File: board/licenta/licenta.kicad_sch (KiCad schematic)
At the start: 44 parts, among them IC1 SAMACSYS_PARTS_NCP186BMX330TAG, IC2 SAMACSYS_PARTS_ESP32-C3-WROOM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, IC3 SAMACSYS_PARTS_BMI085, J1 SAMACSYS_PARTS_USB4110-GF-A, J2 SAMACSYS_PARTS_112A-TAAR-R03_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, Q1 ESP32_WROVER_SPARKFUN-DISCRET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, U1 ESP32-C3-MINI-1, U2 ESP32_WROVER_SPARKFUN-IC-POWE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, U3 DRV2605LDGS, U4 GC9A01_IPS_display_SPI

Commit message: Update schematics w/o PPG
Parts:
- removed IC2: SAMACSYS_PARTS_ESP32-C3-WROOM-02-H4, mini_iot:SAMACSYS_PARTS_ESP32C3WROOM02H4, symbol mini_iot-eagle-import:SAMACSYS_PARTS_ESP32-C3-WROOM-02-H4
- added C1_BAT3: 0.1uF, mini_iot:ESP32_WROVER_EAGLE-LTSPICE_C0402, symbol mini_iot-eagle-import:ESP32_WROVER_EAGLE-LTSPICE_CC0402
- added C1_DRV, C1_DRV1: 1.0uF, mini_iot:ESP32_WROVER_EAGLE-LTSPICE_C0402, symbol mini_iot-eagle-import:ESP32_WROVER_EAGLE-LTSPICE_CC0402
- added C3, C4, C5: 1uF, mini_iot:ESP32_WROVER_EAGLE-LTSPICE_C0402, symbol mini_iot-eagle-import:ESP32_WROVER_EAGLE-LTSPICE_CC0402
- added Q2: 2N7002, Package_TO_SOT_SMD:SOT-23, symbol Transistor_FET:2N7002
- added R1_BTN, R1_ESP1, R2_BTN1, R3_BTN2: 10k, mini_iot:ESP32_WROVER_EAGLE-LTSPICE_R0402, symbol mini_iot-eagle-import:ESP32_WROVER_EAGLE-LTSPICE_RR0402
- added R1_DRV2, R2_DRV2: 2.2k, mini_iot:ESP32_WROVER_EAGLE-LTSPICE_R0402, symbol mini_iot-eagle-import:ESP32_WROVER_EAGLE-LTSPICE_RR0402
- added R1_ESP: 22, mini_iot:ESP32_WROVER_EAGLE-LTSPICE_R0402, symbol mini_iot-eagle-import:ESP32_WROVER_EAGLE-LTSPICE_RR0402
- added SW1: BUTTON_1, Button_Switch_THT:SW_PUSH_LCD_E3_SAxxxx, symbol Switch:SW_MEC_5E
- added SW2: BUTTON_2, Button_Switch_THT:SW_PUSH_LCD_E3_SAxxxx, symbol Switch:SW_MEC_5E
- added SW3: BUTTON_3, Button_Switch_THT:SW_PUSH_LCD_E3_SAxxxx, symbol Switch:SW_MEC_5E
- added U5: A1027, symbol licenta:A1027
- R1_ESP3: value 10k -> 1M
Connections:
- net A1 is gone; now on net ADC_BAT: SJ3.1
- net SDA is gone; now on net 3V3: IC3.9 (SDA/SDI), LED2.6 (SDA)
- net 3V3: now also U1.23 (GPIO9), U1.3 (3V3), U3.10 (VDD), U3.3 (SDA), U4.4 (VDD), C1_BAT3.1, C1_DRV1.2, R1_BTN.2, R1_DRV2.2, R1_ESP.1, R1_ESP1.2, R2_BTN1.2, R2_DRV2.1, R3_BTN2.2; no longer R1_ESP2.2, R1_ESP3.2
- net D+: now also U1.27 (GPIO19/USB_D+)
- net D-: now also U1.26 (GPIO18/USB_D-)
- net GND: now also R1_ESP3.2, U1.1 (GND), U1.11 (GND), U1.14 (GND), U1.2 (GND), U1.36 (GND), U1.37 (GND), U1.38 (GND), U1.39 (GND), U1.40 (GND), U1.41 (GND), U1.42 (GND), U1.43 (GND), U1.44 (GND), U1.45 (GND), U1.46 (GND), U1.47 (GND), U1.48 (GND), U1.49 (GND), U1.50 (GND), U1.51 (GND), U1.52 (GND), U1.53 (GND), U3.8 (GND), U4.1 (GND), U4.12 (GND), U4.5 (GND), U4.6 (GND), C1_BAT3.2, C1_DRV.1, C1_DRV1.1, C3.1, C4.1, C5.1, Q2.2 (S), SW1.1, SW1.2, SW2.1, SW2.2, SW3.1, SW3.2
- net GPIO1: now also U1.13 (GPIO1/ADC1_CH1/XTAL_32K_N)
- net MISO: now also U1.5 (GPIO2/ADC1_CH2), R1_ESP1.1; no longer R1_ESP2.1
- net MOSI: now also U1.21 (GPIO7), U4.10 (SDI)
- net SCK: now also U1.20 (GPIO6), U4.9 (SCK)
- net SCL: now also U1.22 (GPIO8), U3.2 (SCL), R2_DRV2.2
- net SS: no longer J2.P2 (CD/DAT3)
- net SS_SD: now reaches U1.16 (GPIO10)
- net SS_SD: now also J2.P2 (CD/DAT3)
- net TFT_DC: now reaches U1.19 (GPIO5/ADC2_CH0)
- net TFT_DC: now also U4.7 (D/C)
- net SS_TFT: now reaches U1.30 (GPIO20/U0RXD)
- net SS_TFT: now also U4.8 (~{CS})
- net ADC_BAT: now reaches U1.6 (GPIO3/ADC1_CH3)
- net at U3.1 (REG): now also C1_DRV.2
- net IN_DRV: now reaches U3.4 (IN/TRIG)
- net EN_DRV: now reaches U3.5 (EN)
- net OUT+: now reaches U3.7 (OUT+)
- net OUT+: now also U5.1 (OUT+)
- net OUT-: now reaches U3.9 (OUT-)
- net OUT-: now also U5.2 (OUT-)
- net DISP_RST: now reaches U4.11 (~{RESET})
- net LEDK: now reaches U4.2 (LEDK)
- net LEDK: now also Q2.3 (D)
- net at U4.3 (LEDA): now also R1_ESP.2
- net GPIO0: no longer names the net of LED2.5 (INT)
- net NEOPIXEL: no longer names the net of R1_ESP3.1
- net NEOPIXEL: now also R1_ESP2.2, Q2.1 (G)
- new net BUTTON_1: C3.2, R1_BTN.1, SW1.3 (K), SW1.4 (A)
- new net BUTTON_2: C4.2, R2_BTN1.1, SW2.3 (K), SW2.4 (A)
- new net BUTTON_3: C5.2, R3_BTN2.1, SW3.3 (K), SW3.4 (A)
- new net PIN_LED: R1_ESP2.1
- no-connect marks 0 -> 2
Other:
- note added: "Buttons"
- note added: "Haptic motor driver"
- note added: "PPG"
- note removed: "ESP32-C3 WROOM Module"
- note removed: "Haptic motor sensor"
- moved on the sheet: C1, C1_BAT0, C1_SENSOR0, C2_BAT0, CHG_LED0, IC3, J2, JP2, LED2, R1_BAT0, R2_BAT0, R5_ESP1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

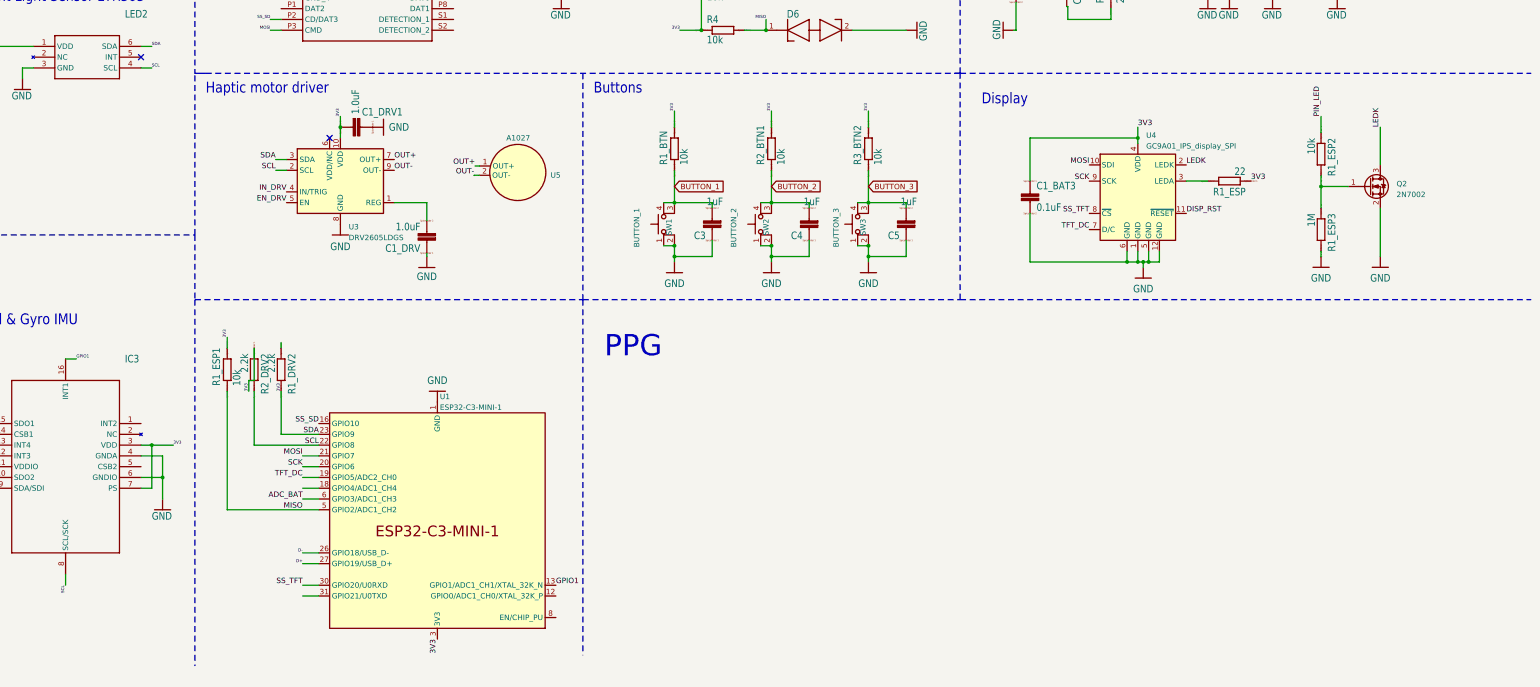
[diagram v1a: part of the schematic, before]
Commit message: Finish schematic draft
Add pin headers for PPG and use 1 pin for reading 3 different buttons
using the ADC. There's not enough space left for the haptic motor
driver.
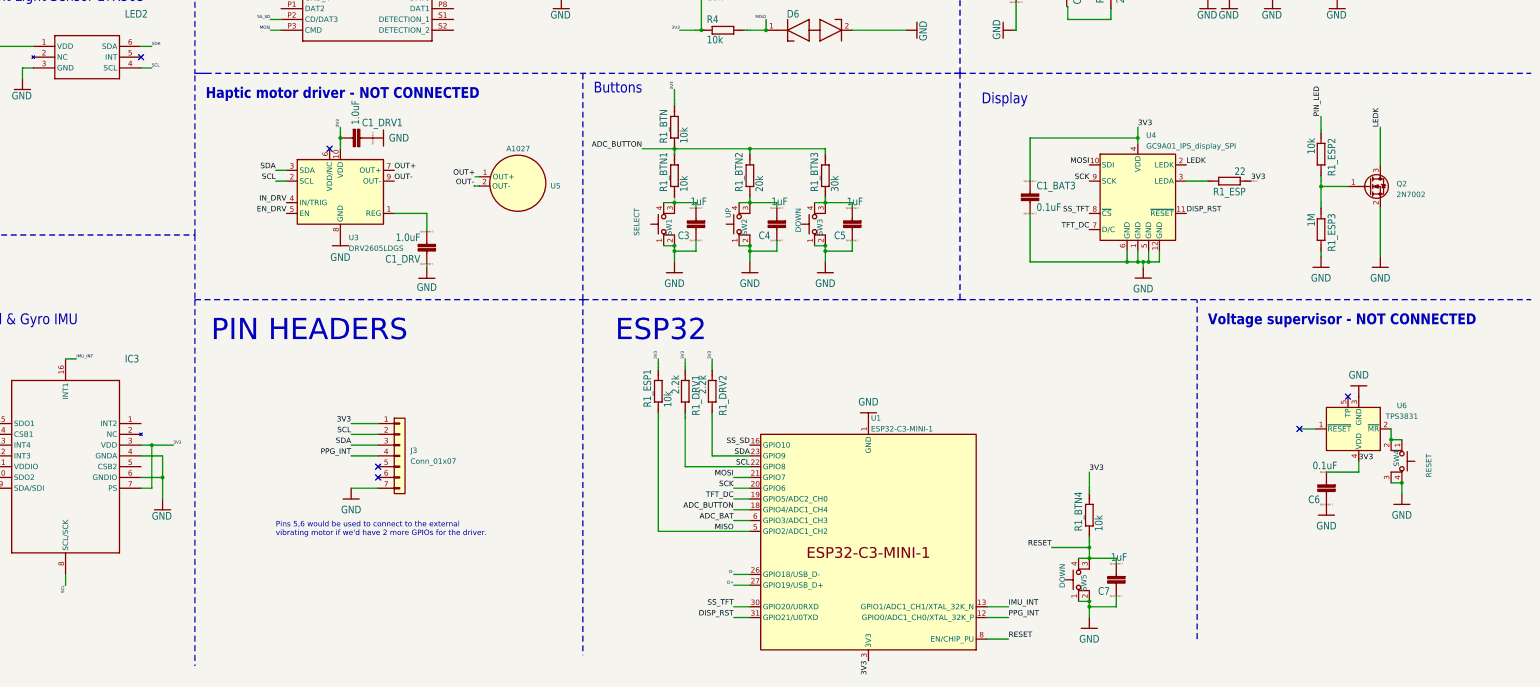
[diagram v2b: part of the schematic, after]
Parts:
- removed R2_BTN1, R3_BTN2: 10k, mini_iot:ESP32_WROVER_EAGLE-LTSPICE_R0402, symbol mini_iot-eagle-import:ESP32_WROVER_EAGLE-LTSPICE_RR0402
- removed R2_DRV2: 2.2k, mini_iot:ESP32_WROVER_EAGLE-LTSPICE_R0402, symbol mini_iot-eagle-import:ESP32_WROVER_EAGLE-LTSPICE_RR0402
- added C6: 0.1uF, mini_iot:ESP32_WROVER_EAGLE-LTSPICE_C0402, symbol mini_iot-eagle-import:ESP32_WROVER_EAGLE-LTSPICE_CC0402
- added C7: 1uF, mini_iot:ESP32_WROVER_EAGLE-LTSPICE_C0402, symbol mini_iot-eagle-import:ESP32_WROVER_EAGLE-LTSPICE_CC0402
- added J3: Conn_01x07, symbol Connector_Generic:Conn_01x07
- added R1_BTN1, R1_BTN4: 10k, mini_iot:ESP32_WROVER_EAGLE-LTSPICE_R0402, symbol mini_iot-eagle-import:ESP32_WROVER_EAGLE-LTSPICE_RR0402
- added R1_BTN2: 20k, mini_iot:ESP32_WROVER_EAGLE-LTSPICE_R0402, symbol mini_iot-eagle-import:ESP32_WROVER_EAGLE-LTSPICE_RR0402
- added R1_BTN3: 30k, mini_iot:ESP32_WROVER_EAGLE-LTSPICE_R0402, symbol mini_iot-eagle-import:ESP32_WROVER_EAGLE-LTSPICE_RR0402
- added R1_DRV1: 2.2k, mini_iot:ESP32_WROVER_EAGLE-LTSPICE_R0402, symbol mini_iot-eagle-import:ESP32_WROVER_EAGLE-LTSPICE_RR0402
- added SW4: RESET, Button_Switch_THT:SW_PUSH_LCD_E3_SAxxxx, symbol Switch:SW_MEC_5E
- added SW5: DOWN, Button_Switch_THT:SW_PUSH_LCD_E3_SAxxxx, symbol Switch:SW_MEC_5E
- added U6: TPS3831, Package_SON:Texas_X2SON-4_1x1mm_P0.65mm, symbol Power_Supervisor:TPS3831
- SW1: value BUTTON_1 -> SELECT
- SW2: value BUTTON_2 -> UP
- SW3: value BUTTON_3 -> DOWN
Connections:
- net 3V3: now also R1_DRV2.1, C6.2, J3.1 (Pin_1), R1_BTN4.2, R1_DRV1.1, U6.4 (VDD); no longer IC3.9 (SDA/SDI), LED2.6 (SDA), R1_DRV2.2, U1.23 (GPIO9), U3.3 (SDA)
- net DISP_RST: now also U1.31 (GPIO21/U0TXD)
- net GND: now also C6.1, C7.1, J3.7 (Pin_7), SW4.3 (K), SW4.4 (A), SW5.1, SW5.2, U6.3 (GND)
- net SCL: now also J3.2 (Pin_2), R1_DRV1.2
- net PPG_INT: now reaches U1.12 (GPIO0/ADC1_CH0/XTAL_32K_P)
- net PPG_INT: now also J3.4 (Pin_4)
- net ADC_BUTTON: now reaches U1.18 (GPIO4/ADC1_CH4)
- net ADC_BUTTON: now also R1_BTN.1, R1_BTN1.2, R1_BTN2.2, R1_BTN3.2
- net RESET: now reaches U1.8 (EN/CHIP_PU)
- net RESET: now also C7.2, R1_BTN4.1, SW5.3 (K), SW5.4 (A)
- net BUTTON_1: no longer names the net of C3.2, SW1.3 (K), SW1.4 (A)
- net BUTTON_1: no longer R1_BTN.1
- net BUTTON_2: no longer names the net of C4.2, SW2.3 (K), SW2.4 (A)
- net BUTTON_2: now also R1_BTN2.1
- net BUTTON_3: no longer names the net of C5.2, SW3.3 (K), SW3.4 (A)
- net BUTTON_3: now also R1_BTN3.1
- net GPIO1 renamed IMU_INT
- new net: SW4.1, SW4.2, U6.2 (~{MR})
- new net SDA: IC3.9 (SDA/SDI), J3.3 (Pin_3), LED2.6 (SDA), R1_DRV2.2, U1.23 (GPIO9), U3.3 (SDA)
- no-connect marks 2 -> 6
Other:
- note added: "ESP32"
- note added: "Haptic motor driver - NOT CONNECTED"
- note added: "PIN HEADERS"
- note added: "Pins 5,6 would be used to connect to the external vibrating motor if we'd have 2 more GPIOs for the driver."
- note added: "Voltage supervisor - NOT CONNECTED"
- note removed: "Haptic motor driver"
- note removed: "PPG"
- moved on the sheet: C1_DRV, C1_DRV1, C3, R1_BTN, R1_DRV2, R1_ESP1, U1, U3, U5

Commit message: Add ESP32 S3 mini to schematic
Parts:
- added U7: ESP32-S3-MINI-1, PCM_Espressif:ESP32-S3-MINI-1, symbol PCM_Espressif:ESP32-S3-MINI-1
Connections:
- net ADC_BAT: now also U7.5 (GPIO1/TOUCH1/ADC1_CH0)
- net ADC_BUTTON: now also U7.7 (GPIO3/TOUCH3/ADC1_CH2)
- net D+: now also U7.24 (GPIO20/U1CTS/ADC2_CH9/CLK_OUT1/USB_D+)
- net D-: now also U7.23 (GPIO19/U1RTS/ADC2_CH8/CLK_OUT2/USB_D-)
- net DISP_RST: now also U7.10 (GPIO6/TOUCH6/ADC1_CH5)
- net EN_DRV: now also U7.17 (GPIO13/TOUCH13/ADC2_CH2/FSPIQ/FSPIIO7/SUBSPIQ)
- net IMU_INT: now also U7.11 (GPIO7/TOUCH7/ADC1_CH6)
- net IN_DRV: now also U7.16 (GPIO12/TOUCH12/ADC2_CH1/FSPICLK/FSPIIO6/SUBSPICLK)
- net MISO: now also U7.33 (SPIDQS/GPIO37/FSPIQ/SUBSPIQ)
- net MOSI: now also U7.31 (SPIIO6/GPIO35/FSPID/SUBSPID)
- net PPG_INT: now also U7.14 (GPIO10/TOUCH10/ADC1_CH9/FSPICS0/FSPIIO4/SUBSPICS0)
- net RESET: now also U7.45 (EN)
- net SCK: now also U7.32 (SPIIO7/GPIO36/FSPICLK/SUBSPICLK)
- net SCL: now also U7.13 (GPIO9/TOUCH9/ADC1_CH8/FSPIHD/SUBSPIHD)
- net SDA: now also U7.12 (GPIO8/TOUCH8/ADC1_CH7/SUBSPICS1)
- net SS_SD: now also U7.29 (SPIIO5/GPIO34/FSPICS0/SUBSPICS0)
- net SS_TFT: now also U7.25 (GPIO21)
- net TFT_DC: now also U7.6 (GPIO2/TOUCH2/ADC1_CH1)
- net LTR_INT: now reaches LED2.5 (INT)
- net LTR_INT: now also U7.15 (GPIO11/TOUCH11/ADC2_CH0/FSPID/FSPIIO5/SUBSPID)
- new net: U7.1 (GND), U7.2 (GND), U7.42 (GND), U7.43 (GND), U7.46 (GND), U7.47 (GND), U7.48 (GND), U7.49 (GND), U7.50 (GND), U7.51 (GND), U7.52 (GND), U7.53 (GND), U7.54 (GND), U7.55 (GND), U7.56 (GND), U7.57 (GND), U7.58 (GND), U7.59 (GND), U7.60 (GND), U7.61 (GND), U7.62 (GND), U7.63 (GND), U7.64 (GND), U7.65 (GND)
- new net RX: U7.36 (MTDO/GPIO40/CLK_OUT2)
- new net TX: U7.35 (MTCK/GPIO39/CLK_OUT3/SUBSPICS1)
- no-connect marks 6 -> 5
